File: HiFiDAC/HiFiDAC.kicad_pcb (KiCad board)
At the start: 4 copper layers, 40 x 40 mm, 130 parts, among them J1 SE, J2 LDIFF, J3 RDIFF, J4 5V, J5 +-15V, J6 I2S, J7 CTRL, U1 KC2520K24.5760, U2 PCM1794A, U3 TPS7A90, U4 OPA1612, U5 OPA1612, U6 OPA1612, U7 OPA1612, U8 OPA1612, U9 MAX14431C/F

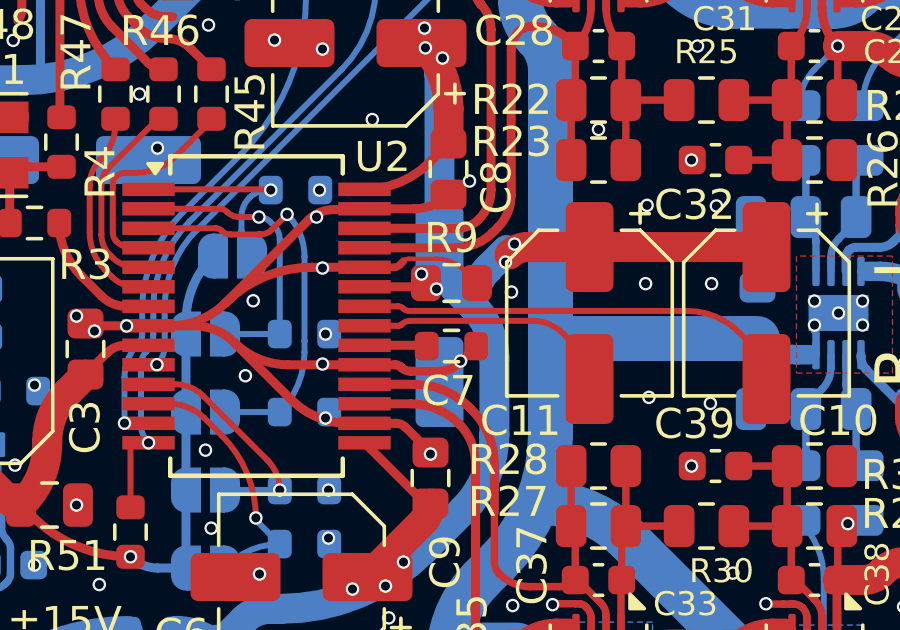
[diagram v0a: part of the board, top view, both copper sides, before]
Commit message: HiFiDAC minor fixes (v1.1)
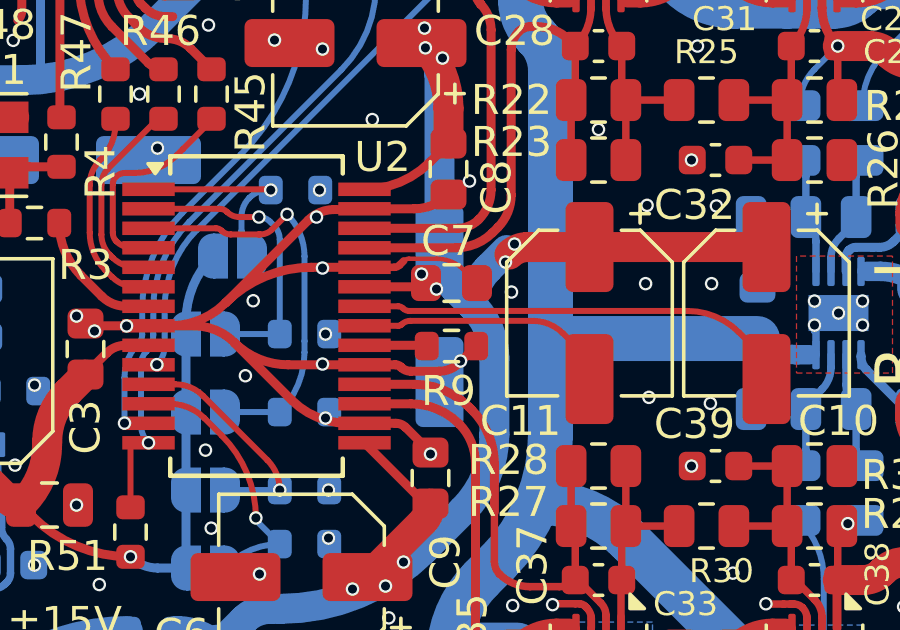
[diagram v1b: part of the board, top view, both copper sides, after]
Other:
- board text added: "Modular Audio HiFi DAC v1.1"
- board text removed: "Modular Audio HiFi DAC"

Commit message: HiFiDAC v2 progress
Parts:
- removed C49, C52: 0.1µF, Capacitor_SMD:C_0603_1608Metric
- removed C50: 100µF 10V 450mΩ, Capacitor_SMD:CP_Elec_6.3x7.7
- removed C51: 10µF 25V, Capacitor_SMD:C_0805_2012Metric
- removed FB2, FB3: MPZ1608B471ATA00, Inductor_SMD:L_0603_1608Metric
- removed JP1: MONO, Jumper:SolderJumper-2_P1.3mm_Open_RoundedPad1.0x1.5mm
- removed JP2: CHSL, Jumper:SolderJumper-2_P1.3mm_Open_RoundedPad1.0x1.5mm
- removed JP3: DEM, Jumper:SolderJumper-2_P1.3mm_Open_RoundedPad1.0x1.5mm
- removed JP4: FMT0, Jumper:SolderJumper-2_P1.3mm_Open_RoundedPad1.0x1.5mm
- removed JP5: FMT1, Jumper:SolderJumper-2_P1.3mm_Open_RoundedPad1.0x1.5mm
- removed R31, R34, R36: 330ΩRS, Resistor_SMD:R_0805_2012Metric
- removed R32, R37, R38, R39, R40, R41, R42, R43, R44: 1kΩRS, Resistor_SMD:R_0805_2012Metric
- removed R33: 4.7kΩRS, Resistor_SMD:R_0805_2012Metric
- removed R35: 470ΩRS, Resistor_SMD:R_0805_2012Metric
- removed R45, R46, R47: 27Ω, Resistor_SMD:R_0603_1608Metric
- removed R48: 0Ω, Resistor_SMD:R_0603_1608Metric
- removed R49, R52, R53: 1kΩ, Resistor_SMD:R_0603_1608Metric
- removed R50, R51: 33kΩ, Resistor_SMD:R_0603_1608Metric
- removed REF**: BW_Logo_5x3.2mm, BW_Logo:BW_Logo_5x3.2mm
- removed U8: OPA1612, Package_SON:WSON-8-1EP_3x3mm_P0.5mm_EP1.2x2mm
- removed U9: MAX14431C/F, Package_SO:QSOP-16_3.9x4.9mm_P0.635mm
- added J8: +-15V, BW_Connectors:Amphenol_MINITEK_0.8_4P_V, F.Cu at (60.1, 103.0)
- added TP1: DEBUG_UART_TX, BW_PassiveMechanical:TP_0603_1608Metric_Fused, F.Cu at (47.7, 86.5)
- added TP2: I2C_~{INT}, BW_PassiveMechanical:TP_0603_1608Metric_Fused, F.Cu at (51.7, 74.0)
- added TP3: I2C_SDA, BW_PassiveMechanical:TP_0603_1608Metric_Fused, F.Cu at (51.7, 76.5)
- added TP4: DEBUG_UART_RX, BW_PassiveMechanical:TP_0603_1608Metric_Fused, F.Cu at (51.7, 79.0)
- added TP5: I2C_SCL, BW_PassiveMechanical:TP_0603_1608Metric_Fused, F.Cu at (51.7, 81.5)
- C1: value 100µF 10V 450mΩ -> 10µF 25V; footprint Capacitor_SMD:CP_Elec_6.3x7.7 -> Capacitor_SMD:C_0805_2012Metric
- C10: value 47µF 20V -> 0.1µF; footprint Capacitor_SMD:CP_Elec_5x5.8 -> Capacitor_SMD:C_0603_1608Metric; moved to B.Cu
- C11: value 47µF 20V -> 0.1µF; footprint Capacitor_SMD:CP_Elec_5x5.8 -> Capacitor_SMD:C_0603_1608Metric
- C12: value 0.1µF -> 100µF 25V; footprint Capacitor_SMD:C_0603_1608Metric -> Capacitor_SMD:CP_Elec_6.3x5.9
- C13: value 10nF -> 100µF 10V; footprint Capacitor_SMD:C_0603_1608Metric -> Capacitor_THT:CP_Radial_D6.3mm_P2.50mm
- C14: value 47µF 20V -> 100µF 25V; footprint Capacitor_SMD:CP_Elec_5x5.8 -> Capacitor_SMD:CP_Elec_6.3x5.9; moved to F.Cu
- C15: value 47µF 20V -> 0.1µF; footprint Capacitor_SMD:CP_Elec_5x5.8 -> Capacitor_SMD:C_0603_1608Metric; moved to F.Cu
- C16: value 0.1µF C0G -> 10µF 50Vs; footprint BW_PassiveMechanical:C_0704_1810Metric -> Capacitor_SMD:C_0805_2012Metric; moved to F.Cu
- C17: value 47µF 20V -> 10µF 50Vs; footprint Capacitor_SMD:CP_Elec_5x5.8 -> Capacitor_SMD:C_0805_2012Metric; moved to F.Cu
- C18: value 10nF C0G -> 220µF 6.3V; footprint Capacitor_SMD:C_0603_1608Metric -> Capacitor_THT:CP_Radial_D5.0mm_P2.00mm; moved to F.Cu
- C19: value 10µF 50Vs -> 1µF 25V; footprint Capacitor_SMD:C_0805_2012Metric -> Capacitor_SMD:C_0603_1608Metric; moved to F.Cu
- C2: value 10µF 50Vs -> 1µF 25V; footprint Capacitor_SMD:C_0805_2012Metric -> Capacitor_SMD:C_0603_1608Metric
- C20: value 100µF 10V 450mΩ -> 0.1µF; footprint Capacitor_SMD:CP_Elec_6.3x7.7 -> Capacitor_SMD:C_0603_1608Metric; moved to F.Cu
- C21, C43, FB1: moved to F.Cu
- C22: value 1µF 25V -> 10µF 50Vs; footprint Capacitor_SMD:C_0603_1608Metric -> Capacitor_SMD:C_0805_2012Metric; moved to F.Cu
- C23: value 2.2nF C0G -> 220µF 6.3V; footprint Capacitor_SMD:C_0603_1608Metric -> Capacitor_THT:CP_Radial_D5.0mm_P2.00mm
- C24: value 2.7nF C0G -> 1µF 25V
- C25, C29: value 2.7nF C0G -> 0.1µF; moved to B.Cu
- C26, C27, C30, C31: value 0.1µF C0G -> 10µF 25V; footprint BW_PassiveMechanical:C_0704_1810Metric -> Capacitor_SMD:C_0805_2012Metric; moved to B.Cu
- C28: value 2.2nF C0G -> 100µF 10V; footprint Capacitor_SMD:C_0603_1608Metric -> Capacitor_THT:CP_Radial_D6.3mm_P2.50mm
- C3: value 0.1µF C0G -> 1µF 25V; footprint BW_PassiveMechanical:C_0704_1810Metric -> Capacitor_SMD:C_0603_1608Metric
- C32: value 2.7nF C0G -> 100µF 10V 450mΩ; footprint Capacitor_SMD:C_0603_1608Metric -> Capacitor_SMD:CP_Elec_6.3x7.7
- C33: value 0.1µF C0G -> 1nF C0G; footprint BW_PassiveMechanical:C_0704_1810Metric -> Capacitor_SMD:C_0603_1608Metric
- C34, C36: value 0.1µF C0G -> 10nF C0G; footprint BW_PassiveMechanical:C_0704_1810Metric -> Capacitor_SMD:C_0603_1608Metric
- C35: value 0.1µF C0G -> 33pF C0G; footprint BW_PassiveMechanical:C_0704_1810Metric -> Capacitor_SMD:C_0603_1608Metric
- C37, C40: value 2.2nF C0G -> 0.1µF C0G; footprint Capacitor_SMD:C_0603_1608Metric -> BW_PassiveMechanical:C_0704_1810Metric
- C38: value 2.7nF C0G -> 1nF C0G
- C39, C42: value 2.7nF C0G -> 10µF 50V; footprint Capacitor_SMD:C_0603_1608Metric -> Capacitor_SMD:C_1206_3216Metric
- C4: value 47µF 20V -> 1µF 25V; footprint Capacitor_SMD:CP_Elec_5x5.8 -> Capacitor_SMD:C_0603_1608Metric; moved to F.Cu
- C41: value 2.7nF C0G -> 0.1µF C0G; footprint Capacitor_SMD:C_0603_1608Metric -> BW_PassiveMechanical:C_0704_1810Metric
- C44: value 0.1µF C0G -> 1nF C0G; footprint BW_PassiveMechanical:C_0704_1810Metric -> Capacitor_SMD:C_0603_1608Metric; moved to F.Cu
- C45: value 0.1µF -> 10nF C0G
- C46: value 0.1µF -> 33pF C0G
- C47: value 1µF -> 10nF C0G; moved to F.Cu
- C48: value 1µF -> 1nF C0G; moved to F.Cu
- C5, C6: value 47µF 20V -> 1µF 25V; footprint Capacitor_SMD:CP_Elec_5x5.8 -> Capacitor_SMD:C_0603_1608Metric
- C7: value 0.1µF C0G -> 0.1µF; footprint BW_PassiveMechanical:C_0704_1810Metric -> Capacitor_SMD:C_0603_1608Metric
- C8: value 0.1µF C0G -> 10nF; footprint BW_PassiveMechanical:C_0704_1810Metric -> Capacitor_SMD:C_0603_1608Metric
- C9: value 0.1µF C0G -> 4.7µF; footprint BW_PassiveMechanical:C_0704_1810Metric -> Capacitor_SMD:C_0603_1608Metric; moved to B.Cu
- J2: value LDIFF -> I2S; footprint BW_Connectors:Amphenol_MINITEK_0.8_2P_V -> BW_Connectors:Amphenol_MINITEK_0.8_6P_V
- J3: value RDIFF -> DIFF_1
- J4: value 5V -> DIFF_2
- J5: value +-15V -> SWD; footprint BW_Connectors:Amphenol_MINITEK_0.8_4P_V -> Connector_PinSocket_1.27mm:PinSocket_1x05_P1.27mm_Vertical_SMD_Pin1Right
- J6: value I2S -> I2C; footprint BW_Connectors:Amphenol_MINITEK_0.8_6P_V -> BW_Connectors:Amphenol_MINITEK_0.8_4P_V
- J7: value CTRL -> 5V; footprint BW_Connectors:Amphenol_MINITEK_0.8_4P_V -> BW_Connectors:Amphenol_MINITEK_0.8_2P_V
- R1: value 100ΩRS -> 2.2Ω; footprint Resistor_SMD:R_0805_2012Metric -> Resistor_SMD:R_0603_1608Metric
- R10: value 10kΩ -> 1kΩLN; moved to F.Cu
- R11, R13: value 10kΩ -> 49.9kΩ
- R15: value 3.12kΩLN -> 22kΩRS; footprint Resistor_SMD:R_0603_1608Metric -> Resistor_SMD:R_0805_2012Metric; moved to F.Cu
- R16: value 1kΩLN -> 3.3kΩRS; footprint Resistor_SMD:R_0603_1608Metric -> Resistor_SMD:R_0805_2012Metric; moved to F.Cu
- R17: value 1kΩRS -> 100ΩRS
- R19, R26: value 330ΩRS -> 4.7kΩRS
- R2: value 100ΩRS -> 0Ω; footprint Resistor_SMD:R_0805_2012Metric -> Resistor_SMD:R_0603_1608Metric
- R20, R25: value 470ΩRS -> 100ΩRS
- R21, R24, R29: value 330ΩRS -> 3.3kΩRS
- R22: value 1kΩRS -> 22kΩRS
- R23: value 4.7kΩRS -> 22kΩRS
- R27: value 1kΩRS -> 4.7kΩRS
- R28: value 4.7kΩRS -> 100ΩRS
- R3: value 0Ω -> 10Ω
- R30: value 470ΩRS -> 22kΩRS
- R4: value 0Ω -> 27Ω
- R5: value 100ΩRS -> 27Ω; footprint Resistor_SMD:R_0805_2012Metric -> Resistor_SMD:R_0603_1608Metric
- R6: value 100ΩRS -> 10kΩ; footprint Resistor_SMD:R_0805_2012Metric -> Resistor_SMD:R_0603_1608Metric
- R7: value 100ΩRS -> 3.12kΩLN; footprint Resistor_SMD:R_0805_2012Metric -> Resistor_SMD:R_0603_1608Metric
- R8: value 100ΩRS -> 1kΩLN; footprint Resistor_SMD:R_0805_2012Metric -> Resistor_SMD:R_0603_1608Metric
- R9: value 10kΩLN -> 3.12kΩLN
- U2: value PCM1794A -> ES9039Q2M; footprint Package_SO:SSOP-28_5.3x10.2mm_P0.65mm -> BW_Active:QFN-32-1EP_5x5mm_P0.5mm_EP3.2x3.2mm
- U3: value TPS7A90 -> STM32C031K6Ux; footprint Package_DFN_QFN:Texas_S-PDSO-N10_EP1.2x2mm -> Package_DFN_QFN:QFN-32-1EP_5x5mm_P0.5mm_EP3.45x3.45mm
- U4: value OPA1612 -> TPS7A87; footprint Package_SON:WSON-8-1EP_3x3mm_P0.5mm_EP1.2x2mm -> Package_DFN_QFN:QFN-20-1EP_4x4mm_P0.5mm_EP2.7x2.7mm
- U5: value OPA1612 -> TLV75101; footprint Package_SON:WSON-8-1EP_3x3mm_P0.5mm_EP1.2x2mm -> BW_Active:WSON-10-1EP_2x2mm_P0.4mm_EP0.9x1.5mm; moved to B.Cu
- moved R2 123.9 mm to (47.7, 74.0), turned to 0 degrees
- moved R6 120.1 mm to (47.7, 84.0), turned to 0 degrees
- moved C28 117.6 mm to (41.8, 122.4)
- moved J2 114.9 mm to (52.9, 90.0), turned to 0 degrees
- moved C32 112.4 mm to (48.3, 114.3)
- moved C14 112.1 mm to (43.0, 100.0), turned to 0 degrees
- moved C27 109.8 mm to (63.7, 130.5)
- moved C25 109.1 mm to (61.1, 129.5), turned to 180 degrees
- moved U5 108.6 mm to (61.1, 127.4), turned to 0 degrees
- moved R1 105.5 mm to (82.6, 157.8), turned to 0 degrees
- moved C31 103.5 mm to (63.7, 127.0), turned to 90 degrees
- moved C29 103.1 mm to (65.5, 126.7), turned to 90 degrees
- moved C26 101.1 mm to (65.8, 130.0)
- moved C30 98.7 mm to (60.9, 125.1), turned to 180 degrees
- moved R12 90.6 mm to (58.8, 130.3), turned to -90 degrees
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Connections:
- C1 pad 1: +3.3V -> Net-(U2-AVDD)
- C1 pad 2: GND -> Net-(C1-Pad2)
- C10 pad 1: +5V -> GND
- C10 pad 2: Net-(U2-VCOML) -> +3.3VD
- C11 pad 1: +5V -> Net-(J5-Pin_5)
- C11 pad 2: Net-(U2-VCOMR) -> GND
- C12 pad 1: +3.3VD -> +15V
- C13 pad 1: +3.3VD -> +5V
- C14 pad 1: +15V -> GND
- C14 pad 2: GND -> -15V
- C15 pad 1: +5V -> /3.3V Supply/3.3VDAC1
- C15 pad 2: GND -> Net-(U4B-FB)
- C17 pad 1: GND -> /3.3V Supply/3.3VDAC1
- C17 pad 2: -15V -> GND
- C18 pad 1: +3.3V -> /3.3V Supply/3.3VDAC1
- C18 pad 2: Net-(U3-FB) -> GND
- C19 pad 1: +3.3V -> Net-(U4B-NR/SS)
- C2 pad 1: +3.3V -> Net-(U2-AVDD)
- C20 pad 1: Net-(U3-EN) -> /3.3V Supply/3.3VDAC2
- C20 pad 2: GND -> Net-(U4A-FB)
- C21 pad 1: Net-(U3-EN) -> +5V
- C22 pad 1: Net-(U3-NR/SS) -> /3.3V Supply/3.3VDAC2
- C23 pad 1: /I-V Stage/IL- -> /3.3V Supply/3.3VDAC2
- C23 pad 2: Net-(C23-Pad2) -> GND
- C24 pad 1: /Differential Amp/VL- -> Net-(U4A-NR/SS)
- C24 pad 2: Net-(U5A--) -> GND
- C25 pad 1: GND -> /3.3V Supply/3.3VA
- C25 pad 2: Net-(U5A--) -> Net-(U5A-FB)
- C26 pad 1: GND -> +5V
- C26 pad 2: +15V -> GND
- C27 pad 1: GND -> /3.3V Supply/3.3VA
- C27 pad 2: +15V -> GND
- C28 pad 1: /I-V Stage/IL+ -> /3.3V Supply/3.3VA
- C28 pad 2: Net-(C28-Pad2) -> GND
- C29 pad 1: /Differential Amp/VL+ -> +3.3VD
- C29 pad 2: Net-(U5B--) -> Net-(U5B-FB)
- C3 pad 1: +3.3V -> Net-(U2-DVDD)
- C30 pad 1: -15V -> +5V
- C31 pad 1: -15V -> +3.3VD
- C32 pad 1: GND -> +3.3VD
- C32 pad 2: Net-(U5B--) -> GND
- C33 pad 1: GND -> /I-V Stage/I1+
- C33 pad 2: +15V -> Net-(C33-Pad2)
- C34 pad 2: +15V -> /I-V Stage/V1-
- C35 pad 1: -15V -> Net-(U6A--)
- C35 pad 2: GND -> Net-(C33-Pad2)
- C36 pad 1: -15V -> GND
- C36 pad 2: GND -> /I-V Stage/V1+
- C37 pad 1: /I-V Stage/IR- -> GND
- C37 pad 2: Net-(C37-Pad2) -> +15V
- C38 pad 1: /Differential Amp/VR- -> /I-V Stage/I1-
- C38 pad 2: Net-(U7A--) -> Net-(C38-Pad2)
- C39 pad 1: GND -> +15V
- C39 pad 2: Net-(U7A--) -> -15V
- C4 pad 1: +5V -> /3.3V Supply/3.3VA
- C40 pad 1: /I-V Stage/IR+ -> -15V
- C40 pad 2: Net-(C40-Pad2) -> GND
- C41 pad 1: /Differential Amp/VR+ -> GND
- C41 pad 2: Net-(U7B--) -> +15V
- C42 pad 1: GND -> +15V
- C42 pad 2: Net-(U7B--) -> -15V
- C43 pad 1: GND -> -15V
- C43 pad 2: +15V -> GND
- C44 pad 1: -15V -> /I-V Stage/I2+
- C44 pad 2: GND -> Net-(C44-Pad2)
- C45 pad 1: /Digital Interface/VDD_EXT -> GND
- C45 pad 2: /Digital Interface/GND_EXT -> /I-V Stage/V2-
- C46 pad 1: +3.3VD -> Net-(U7A--)
- C46 pad 2: GND -> Net-(C44-Pad2)
- C47 pad 1: /Digital Interface/MUTE -> GND
- C47 pad 2: GND -> /I-V Stage/V2+
- C48 pad 1: /Digital Interface/~{RST} -> /I-V Stage/I2-
- C48 pad 2: GND -> Net-(C48-Pad2)
- C5 pad 1: +5V -> /3.3V Supply/3.3VDAC1
- C6 pad 1: +5V -> /3.3V Supply/3.3VDAC2
- C7 pad 1: GND -> +3.3VD
- C7 pad 2: +5V -> GND
- C8 pad 1: GND -> +3.3VD
- C8 pad 2: +5V -> GND
- C9 pad 2: +5V -> +3.3VD
- FB1 pad 1: +5V -> +3.3VD
- FB1 pad 2: Net-(U3-EN) -> Net-(U2-AVDD)
- J1 pad 1: Net-(J1-Pin_1) -> /I-V Stage/V2+
- J1 pad 4: Net-(J1-Pin_4) -> /I-V Stage/V1+
- J2 pad 1: Net-(J2-Pin_1) -> unconnected-(J2-Pin_1-Pad1)
- J2 pad 2: Net-(J2-Pin_2) -> /BCK
- J3 pad 1: Net-(J3-Pin_1) -> /I-V Stage/V1+
- J3 pad 2: Net-(J3-Pin_2) -> /I-V Stage/V1-
- J4 pad 1: +5V -> /I-V Stage/V2+
- J4 pad 2: GND -> /I-V Stage/V2-
- J5 pad 1: +15V -> +3.3VD
- J5 pad 2: GND -> /SWCLK
- J5 pad 4: -15V -> /SWDIO
- J6 pad 1: /Digital Interface/VDD_EXT -> Net-(J6-Pin_1)
- J6 pad 4: Net-(J6-Pin_4) -> GND
- J7 pad 1: Net-(J7-Pin_1) -> +5V
- J7 pad 2: Net-(J7-Pin_2) -> GND
- R1 pad 1: Net-(J1-Pin_4) -> GND
- R1 pad 2: /Differential Amp/VL_SE -> Net-(C1-Pad2)
- R10 pad 1: /MONO -> Net-(U4A-FB)
- R11 pad 1: /CHSL -> /3.3V Supply/3.3VA
- R11 pad 2: GND -> Net-(U5A-FB)
- R12 pad 1: /DEM -> Net-(U5A-FB)
- R13 pad 1: /FMT0 -> +3.3VD
- R13 pad 2: GND -> Net-(U5B-FB)
- R14 pad 1: /FMT1 -> Net-(U5B-FB)
- R15 pad 1: +3.3V -> /I-V Stage/I1+
- R15 pad 2: Net-(U3-FB) -> Net-(C33-Pad2)
- R16 pad 1: Net-(U3-FB) -> /I-V Stage/I1+
- R16 pad 2: GND -> Net-(C33-Pad2)
- R17 pad 1: /I-V Stage/IL- -> Net-(C33-Pad2)
- R17 pad 2: Net-(C23-Pad2) -> /I-V Stage/V1-
- R18 pad 1: /I-V Stage/IL- -> Net-(U6A--)
- R18 pad 2: Net-(C23-Pad2) -> Net-(C33-Pad2)
- R19 pad 1: /Differential Amp/VL- -> Net-(C38-Pad2)
- R19 pad 2: Net-(U5A--) -> Net-(U6A--)
- R2 pad 1: Net-(J1-Pin_1) -> Net-(J2-Pin_5)
- R2 pad 2: /Differential Amp/VR_SE -> Net-(U1-CLK)
- R20 pad 1: Net-(C23-Pad2) -> Net-(C38-Pad2)
- R20 pad 2: Net-(U5A--) -> /I-V Stage/V1+
- R21 pad 1: GND -> /I-V Stage/I1-
- R21 pad 2: Net-(U5A--) -> Net-(C38-Pad2)
- R22 pad 1: /I-V Stage/IL+ -> /I-V Stage/I1-
- R22 pad 2: Net-(C28-Pad2) -> Net-(C38-Pad2)
- R23 pad 1: /I-V Stage/IL+ -> /I-V Stage/I2+
- R23 pad 2: Net-(C28-Pad2) -> Net-(C44-Pad2)
- R24 pad 1: /Differential Amp/VL+ -> /I-V Stage/I2+
- R24 pad 2: Net-(U5B--) -> Net-(C44-Pad2)
- R25 pad 1: Net-(C28-Pad2) -> Net-(C44-Pad2)
- R25 pad 2: Net-(U5B--) -> /I-V Stage/V2-
- R26 pad 1: GND -> Net-(U7A--)
- R26 pad 2: Net-(U5B--) -> Net-(C44-Pad2)
- R27 pad 1: /I-V Stage/IR- -> Net-(C48-Pad2)
- R27 pad 2: Net-(C37-Pad2) -> Net-(U7A--)
- R28 pad 1: /I-V Stage/IR- -> Net-(C48-Pad2)
- R28 pad 2: Net-(C37-Pad2) -> /I-V Stage/V2+
- R29 pad 1: /Differential Amp/VR- -> /I-V Stage/I2-
- R29 pad 2: Net-(U7A--) -> Net-(C48-Pad2)
- R3 pad 1: Net-(U1-CLK) -> /BCK
- R3 pad 2: Net-(U2-SCK) -> Net-(U2-DATA_CLK)
- R30 pad 1: Net-(C37-Pad2) -> /I-V Stage/I2-
- R30 pad 2: Net-(U7A--) -> Net-(C48-Pad2)
- R4 pad 1: /Digital Interface/SCK -> /LRCK
- R4 pad 2: Net-(U1-CLK) -> Net-(U2-DATA1)
- R5 pad 1: Net-(J2-Pin_1) -> /DATA
- R5 pad 2: /Differential Amp/VL+ -> Net-(U2-DATA2)
- R6 pad 1: Net-(J2-Pin_2) -> +3.3VD
- R6 pad 2: /Differential Amp/VL- -> Net-(J5-Pin_5)
- R7 pad 1: Net-(J3-Pin_1) -> /3.3V Supply/3.3VDAC1
- R7 pad 2: /Differential Amp/VR+ -> Net-(U4B-FB)
- R8 pad 1: Net-(J3-Pin_2) -> Net-(U4B-FB)
- R8 pad 2: /Differential Amp/VR- -> GND
- R9 pad 1: Net-(U2-IREF) -> /3.3V Supply/3.3VDAC2
- R9 pad 2: GND -> Net-(U4A-FB)
- U2 pad 1: /MONO -> /3.3V Supply/3.3VDAC1
- U2 pad 10: /Digital Interface/MUTE -> Net-(U2-AVDD)
- U2 pad 11: /FMT0 -> GND
- U2 pad 12: /FMT1 -> Net-(U2-DATA_CLK)
- U2 pad 13: /ZERO -> Net-(U2-DATA1)
- U2 pad 14: /Digital Interface/~{RST} -> Net-(U2-DATA2)
- U2 pad 15: +5V -> Net-(U2-SCLK/SCL/HW1)
- U2 pad 16: GND -> Net-(U2-MOSI/SDA/HW0)
- U2 pad 17: /I-V Stage/IR+ -> GND
- U2 pad 18: /I-V Stage/IR- -> Net-(U2-CHIP_EN)
- U2 pad 19: GND -> Net-(U2-SS/ADDR1/HW2)
- U2 pad 2: /CHSL -> /I-V Stage/I1-
- U2 pad 20: Net-(U2-IREF) -> Net-(U2-MISO/ADDR0/MUTE_CTRL)
- U2 pad 21: Net-(U2-VCOMR) -> Net-(U2-GPIO1)
- U2 pad 22: Net-(U2-VCOML) -> /GPIO2
- U2 pad 23: +5V -> /GPIO3
- U2 pad 24: GND -> /GPIO4
- U2 pad 25: /I-V Stage/IL+ -> Net-(U2-GPIO5)
- U2 pad 26: /I-V Stage/IL- -> Net-(U2-GPIO6)
- U2 pad 27: GND -> /GPIO7
- U2 pad 28: +5V -> unconnected-(U2-GPIO8-Pad28)
- U2 pad 3: /DEM -> /I-V Stage/I1+
- U2 pad 4: /Digital Interface/LRCK -> GND
- U2 pad 5: /Digital Interface/DATA -> GND
- U2 pad 6: /Digital Interface/BCK -> /I-V Stage/I2-
- U2 pad 7: Net-(U2-SCK) -> /I-V Stage/I2+
- U2 pad 8: GND -> /3.3V Supply/3.3VDAC2
- U2 pad 9: +3.3V -> Net-(U2-DVDD)
- U3 pad 1: +3.3V -> unconnected-(U3-PB9-Pad1)
- U3 pad 10: Net-(U3-EN) -> Net-(U2-CHIP_EN)
- U3 pad 11: GND -> Net-(U2-SS/ADDR1/HW2)
- U3 pad 2: +3.3V -> Net-(U3-PC14)
- U3 pad 3: Net-(U3-FB) -> unconnected-(U3-PC15-Pad3)
- U3 pad 4: GND -> +3.3VD
- U3 pad 5: unconnected-(U3-PG-Pad5) -> GND
- U3 pad 6: Net-(U3-EN) -> Net-(J5-Pin_5)
- U3 pad 7: Net-(U3-EN) -> unconnected-(U3-PA0-Pad7)
- U3 pad 8: Net-(U3-NR/SS) -> Net-(U2-SCLK/SCL/HW1)
- U3 pad 9: Net-(U3-EN) -> Net-(U2-MOSI/SDA/HW0)
- U4 pad 1: Net-(C23-Pad2) -> +5V
- U4 pad 2: /I-V Stage/IL- -> +5V
- U4 pad 4: -15V -> +5V
- U4 pad 5: GND -> +5V
- U4 pad 6: /I-V Stage/IL+ -> +5V
- U4 pad 7: Net-(C28-Pad2) -> Net-(U4B-NR/SS)
- U4 pad 8: +15V -> +5V
- U4 pad 9: -15V -> unconnected-(U4B-PG-Pad9)
- U5 pad 1: /Differential Amp/VL- -> Net-(U5A-FB)
- U5 pad 2: Net-(U5A--) -> GND
- U5 pad 3: GND -> +5V
- U5 pad 4: -15V -> GND
- U5 pad 5: GND -> +5V
- U5 pad 6: Net-(U5B--) -> +5V
- U5 pad 7: /Differential Amp/VL+ -> Net-(U5B-FB)
- U5 pad 8: +15V -> +3.3VD
- U5 pad 9: -15V -> +5V
- U6 pad 1: Net-(C37-Pad2) -> Net-(C33-Pad2)
- U6 pad 2: /I-V Stage/IR- -> Net-(U6A--)
- U6 pad 5: GND -> /I-V Stage/I1+
- U6 pad 6: /I-V Stage/IR+ -> /I-V Stage/I1-
- U6 pad 7: Net-(C40-Pad2) -> Net-(C38-Pad2)
- U7 pad 1: /Differential Amp/VR- -> Net-(C44-Pad2)
- U7 pad 5: GND -> /I-V Stage/I2+
- U7 pad 6: Net-(U7B--) -> /I-V Stage/I2-
- U7 pad 7: /Differential Amp/VR+ -> Net-(C48-Pad2)
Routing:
- net -15V: track 82.8 -> 0.00 mm, vias 37 -> 0
- net +15V: track 80.7 -> 0.00 mm, vias 13 -> 0
- net +5V: track 76.8 -> 0.00 mm, vias 15 -> 0
- net GND: track 76.8 -> 0.00 mm, vias 124 -> 0
- net +3.3V: track 35.0 -> 0.00 mm, vias 4 -> 0
- net +3.3VD: track 29.7 -> 0.00 mm, vias 8 -> 0
- net /Digital Interface/~{RST}: track 26.3 -> 0.00 mm, vias 1 -> 0
- net /I-V Stage/IL-: track 24.1 -> 0.00 mm
- net /ZERO: track 23.1 -> 0.00 mm, vias 1 -> 0
- net /Digital Interface/MUTE: track 22.6 -> 0.00 mm, vias 1 -> 0
- net /I-V Stage/IR+: track 22.4 -> 0.00 mm
- net Net-(U3-EN): track 20.8 -> 0.00 mm
- net /I-V Stage/IL+: track 19.0 -> 0.00 mm
- net /I-V Stage/IR-: track 18.1 -> 0.00 mm
- net /Differential Amp/VL-: track 16.7 -> 0.00 mm, vias 1 -> 0
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- removed copper zone on B.Cu, net -15V
- removed copper zone on F.Cu, net -15V
- removed copper zone on B.Cu, net /Digital Interface/GND_EXT
- removed copper zone on F.Cu, net /Digital Interface/GND_EXT
- removed copper zone on In1.Cu, net /Digital Interface/GND_EXT
- removed copper zone on In2.Cu, net /Digital Interface/GND_EXT
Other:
- board text removed: "+"
- board text removed: "5V"
- board text removed: "CHSL"
- board text removed: "CTRL"
- board text removed: "DEM"
- board text removed: "FMT 0 1"
- board text removed: "I2S +"
- board text removed: "L"
- board text removed: "MONO"
- board text removed: "Modular Audio HiFi DAC v1.1"
- board text removed: "R"
- board text removed: "kitty was here"
- board text removed: "±15V"

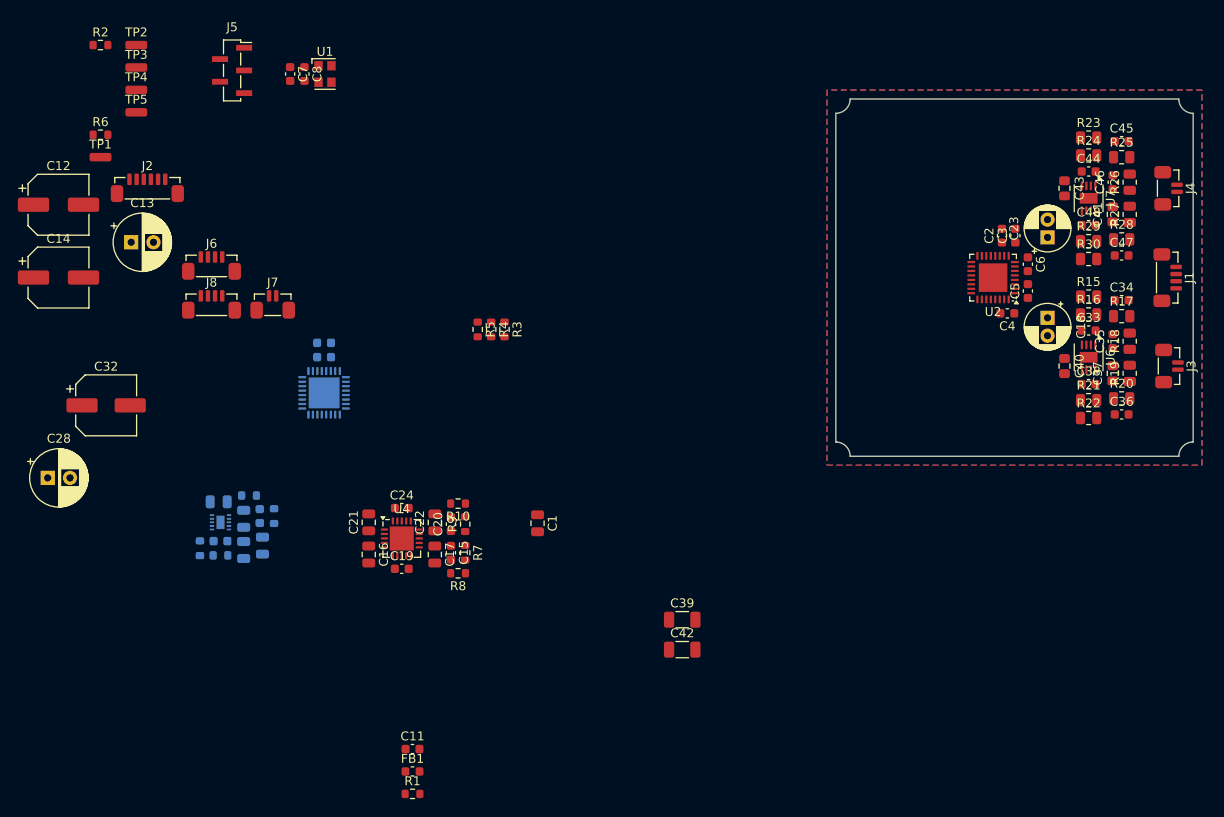
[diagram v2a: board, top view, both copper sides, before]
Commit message: HiFiDAC v2 layout+route progress
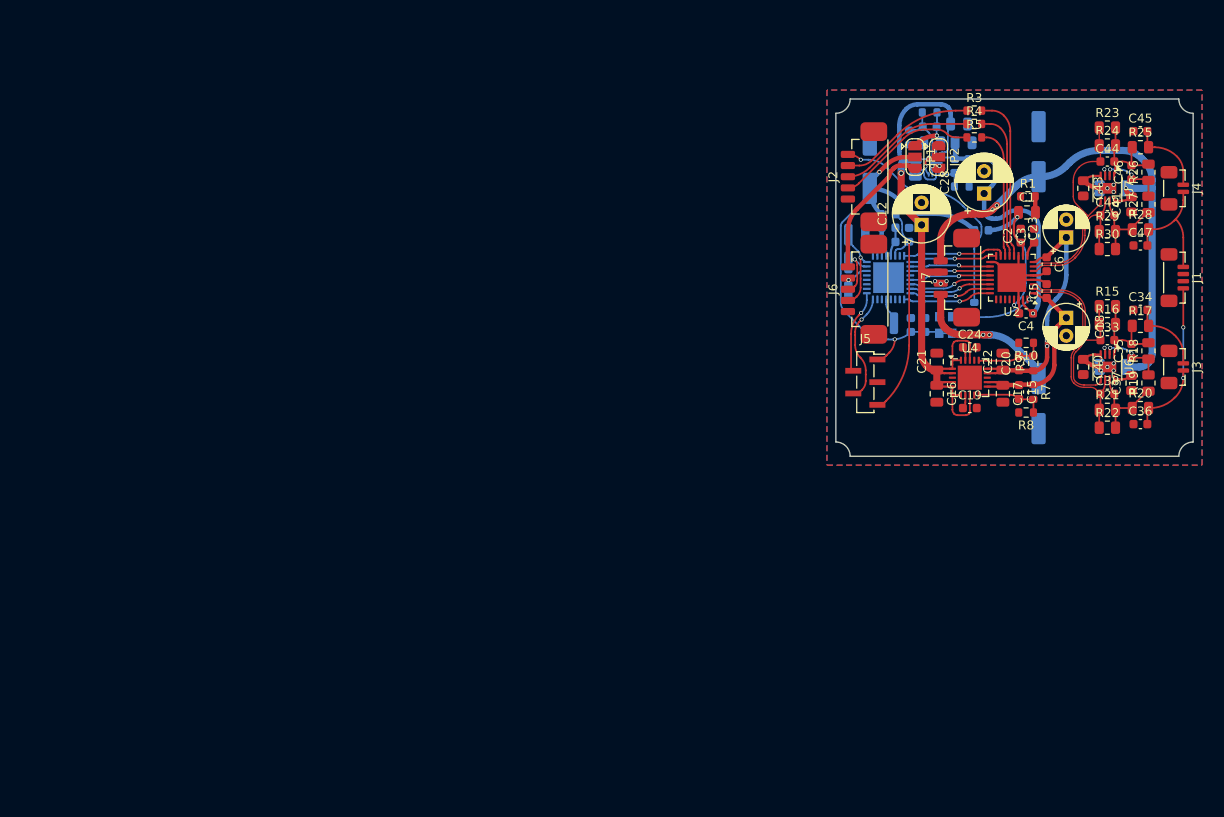
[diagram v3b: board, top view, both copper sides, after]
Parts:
- removed the J7 at (66.9, 103.0)
- added JP1: VD_SEL, Jumper:SolderJumper-3_P1.3mm_Open_RoundedPad1.0x1.5mm, F.Cu at (138.9, 86.5)
- added JP2: VD_REG_EN, Jumper:SolderJumper-3_P1.3mm_Open_RoundedPad1.0x1.5mm, F.Cu at (141.5, 86.5)
- C11, C14, C32, C39, C42, C7, C8, FB1, R2, R6, TP1, TP2, TP3, TP4, TP5, U1: moved to B.Cu
- C13: renamed from C12; moved to B.Cu
- J2: footprint BW_Connectors:Amphenol_MINITEK_0.8_6P_V -> BW_Connectors:Amphenol_MINITEK_WTB_1.25_5P_V
- J6: footprint BW_Connectors:Amphenol_MINITEK_0.8_4P_V -> BW_Connectors:Amphenol_MINITEK_WTB_1.25_5P_V
- J7: renamed from J8; value +-15V -> PWR; footprint BW_Connectors:Amphenol_MINITEK_0.8_4P_V -> BW_Connectors:Amphenol_MINITEK_WTB_1.25_4P_V
- moved C14 110.6 mm to (152.7, 114.1), turned to 90 degrees
- moved C13 109.9 mm to (152.7, 85.9), turned to 90 degrees
- moved C28 109.6 mm to (146.6, 90.6), turned to 90 degrees
- moved R2 102.2 mm to (145.5, 103.6), turned to -90 degrees
- moved R1 96.0 mm to (151.5, 90.9)
- moved R11 94.5 mm to (144.9, 87.5), turned to -90 degrees
- moved R12 94.4 mm to (144.1, 89.8), turned to 0 degrees
- moved C27 92.6 mm to (144.3, 84.9), turned to 0 degrees
- moved C25 92.3 mm to (143.3, 87.5), turned to -90 degrees
- moved C26 91.2 mm to (143.8, 82.8), turned to 0 degrees
- moved C32 89.7 mm to (133.8, 87.3), turned to 90 degrees
- moved U5 89.5 mm to (141.2, 87.5), turned to 90 degrees
- moved TP4 88.8 mm to (136.5, 105.1), turned to -90 degrees
- moved R6 88.7 mm to (135.9, 92.9)
- moved C12 88.5 mm to (139.6, 94.1), turned to 90 degrees
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- renumbered C13 to C12
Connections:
- C29 pad 1: +3.3VD -> Net-(JP1-A)
- C31 pad 1: +3.3VD -> Net-(JP1-A)
- J1 pad 1: /I-V Stage/V2+ -> /I-V Stage/V1+
- J1 pad 4: /I-V Stage/V1+ -> /I-V Stage/V2+
- J2 pad 1: unconnected-(J2-Pin_1-Pad1) -> Net-(J2-Pin_1)
- J2 pad 5: Net-(J2-Pin_5) -> GND
- J6 pad 1: Net-(J6-Pin_1) -> /3.3V_EXT
- J6 pad 4: GND -> Net-(J6-Pin_4)
- J7 pad 2: GND -> +5V
- R13 pad 1: +3.3VD -> Net-(JP1-A)
- R2 pad 1: Net-(J2-Pin_5) -> Net-(J2-Pin_1)
- TP2 pad 1: Net-(J6-Pin_3) -> Net-(J6-Pin_4)
- TP3 pad 1: Net-(J6-Pin_2) -> Net-(J6-Pin_3)
- TP5 pad 1: Net-(J6-Pin_1) -> Net-(J6-Pin_2)
- U2 pad 25: Net-(U2-GPIO5) -> unconnected-(U2-GPIO5-Pad25)
- U2 pad 26: Net-(U2-GPIO6) -> unconnected-(U2-GPIO6-Pad26)
- U2 pad 27: /GPIO7 -> unconnected-(U2-GPIO7-Pad27)
- U3 pad 18: Net-(U2-GPIO5) -> unconnected-(U3-PA8-Pad18)
- U3 pad 19: Net-(U2-GPIO6) -> unconnected-(U3-PA9/NC-Pad19)
- U3 pad 20: /GPIO7 -> unconnected-(U3-PC6-Pad20)
- U3 pad 30: Net-(J6-Pin_1) -> Net-(J6-Pin_2)
- U3 pad 31: Net-(J6-Pin_2) -> Net-(J6-Pin_3)
- U3 pad 32: Net-(J6-Pin_3) -> Net-(J6-Pin_4)
- U5 pad 5: +5V -> Net-(JP2-C)
- U5 pad 8: +3.3VD -> Net-(JP1-A)
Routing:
- net +5V: track 0.00 -> 76.6 mm, vias 0 -> 1
- net +15V: track 0.00 -> 63.7 mm, vias 0 -> 3
- net +3.3VD: track 0.00 -> 59.6 mm, vias 0 -> 2
- net /3.3V Supply/3.3VA: track 0.00 -> 33.3 mm, vias 0 -> 1
- net /3.3V Supply/3.3VDAC2: track 0.00 -> 28.7 mm, vias 0 -> 2
- net -15V: track 0.00 -> 27.5 mm, vias 0 -> 12
- net Net-(J2-Pin_1): track 0.00 -> 26.5 mm, vias 0 -> 1
- net GND: track 0.00 -> 26.2 mm, vias 0 -> 7
- net Net-(J5-Pin_5): track 0.00 -> 25.6 mm, vias 0 -> 1
- net /I-V Stage/I2+: track 0.00 -> 24.6 mm
- net /I-V Stage/I1+: track 0.00 -> 24.5 mm
- net /I-V Stage/I1-: track 0.00 -> 24.1 mm
- net /3.3V Supply/3.3VDAC1: track 0.00 -> 21.5 mm
- net Net-(U2-DATA_CLK): track 0.00 -> 18.6 mm
- net /I-V Stage/V1+: track 0.00 -> 18.4 mm, vias 0 -> 2
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
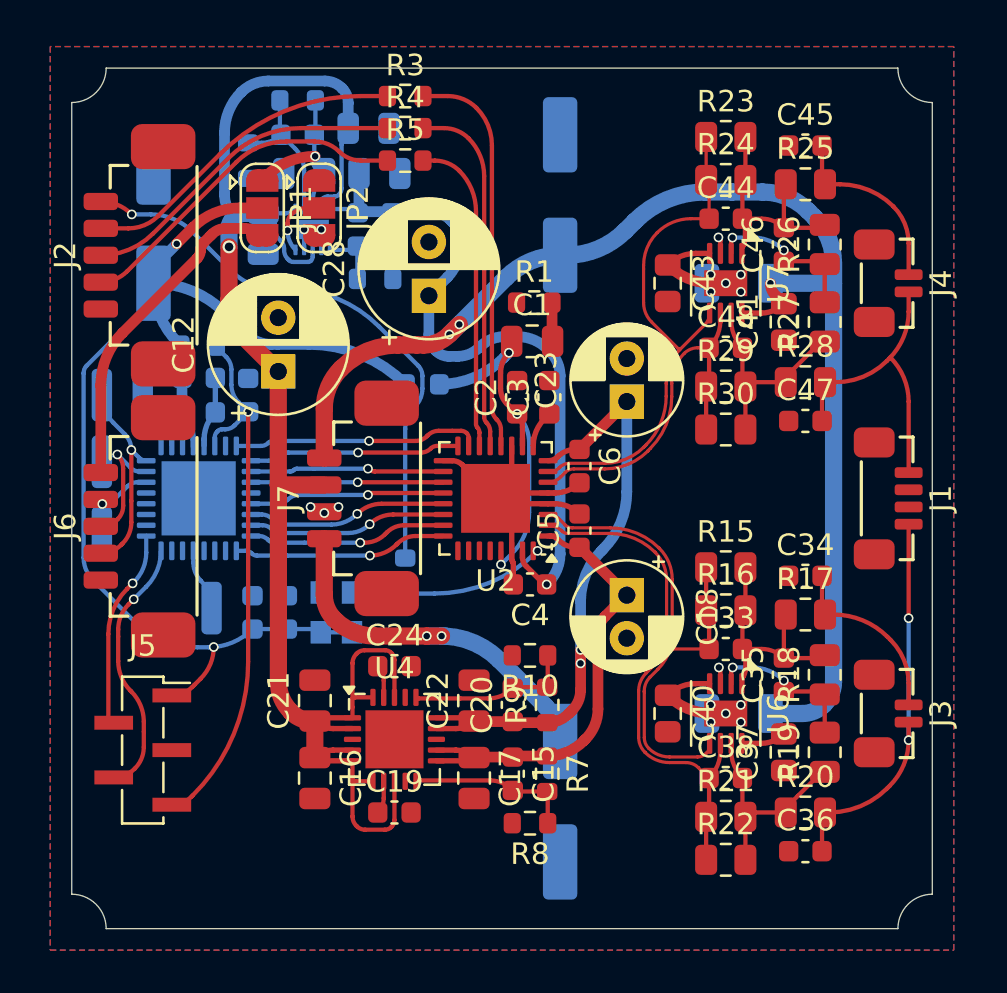
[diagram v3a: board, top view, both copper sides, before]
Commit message: HiFiDAC v2 ordered version
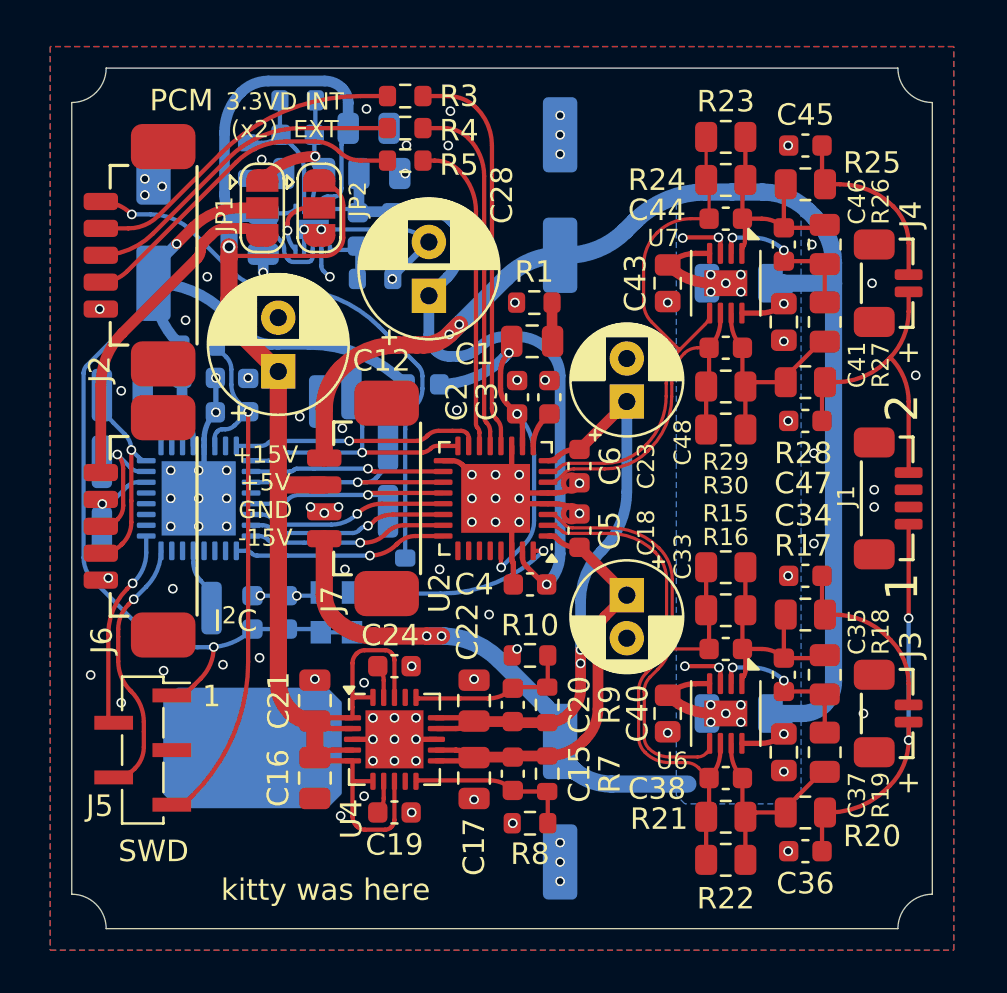
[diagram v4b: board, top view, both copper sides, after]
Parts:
- added REF**: BW_Logo_7.5x4.8mm, BW_Logo:BW_Logo_7.5x4.8mm, B.Cu at (138.4, 111.6)
- added TP6: SCLK, BW_PassiveMechanical:TP_0603_1608Metric_Fused, B.Cu at (141.5, 95.5)
- added TP7: MOSI, BW_PassiveMechanical:TP_0603_1608Metric_Fused, B.Cu at (143.0, 95.1)
- added TP8: SS, BW_PassiveMechanical:TP_0603_1608Metric_Fused, B.Cu at (144.7, 97.5)
- added TP9: MISO, BW_PassiveMechanical:TP_0603_1608Metric_Fused, B.Cu at (144.7, 100.6)
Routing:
- net GND: track 26.2 -> 52.9 mm, vias 7 -> 109
- net +5V: track 76.6 -> 85.7 mm
- net -15V: track 27.5 -> 35.1 mm
- net Net-(U2-MOSI/SDA/HW0): track 9.78 -> 12.7 mm
- net Net-(U2-SS/ADDR1/HW2): track 8.92 -> 11.5 mm
- net Net-(U2-SCLK/SCL/HW1): track 11.5 -> 13.4 mm
- net Net-(U2-MISO/ADDR0/MUTE_CTRL): track 9.05 -> 10.6 mm
- net +15V: track 63.7 -> 64.5 mm, vias 3 -> 4
- net Net-(U1-CLK): track 9.33 -> 9.90 mm
- added copper zone on B.Cu, net -15V
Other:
- board text added: "+"
- board text added: "+15V +5V GND -15V"
- board text added: "1"
- board text added: "2"
- board text added: "3.3VD INT (x2) EXT"
- board text added: "I^{2}C"
- board text added: "Modular Audio HiFiDAC v2"
- board text added: "PCM"
- board text added: "SWD"
- board text added: "kitty was here"

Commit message: HiFiDAC halved I-V gain
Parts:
- C33, C38, C44, C48: value 1nF C0G -> 1.5nF C0G
- R16, R21, R24, R29: value 3.3kΩRS -> 1.5kΩRS
